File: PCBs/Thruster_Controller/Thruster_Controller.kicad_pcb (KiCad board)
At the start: 4 copper layers, 108 x 54 mm, 163 parts, among them J1 PHASE_A, J2 PHASE_B, J3 PHASE_C, J4 Big Conn, J5 Pogo Conn, J6 Conn CAN, J7 PWR_IN, Q1 SIZF906DT, Q2 SIZF906DT, Q3 SIZF906DT, SW1 SW_Push, SW2 SW_Push, U1 DRV8305, U2 RTQ2569-50GQW, U3 MCP2515, U4 LMR16006XDDC, U5 TMS320F28027F, U6 SN74LVC2G07, U7 SN74LVC2G07, U8 MCP2562, Y1 20MHz

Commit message: Layout
- Trying out different layout approaches
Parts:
- removed D4: D_Schottky_ALT, Diodes_SMD:D_SOD-123F
- removed D5, D6, D7, D8: BLUE, LEDs:LED_0805
- removed H3, H4: MountingHole, Mounting_Holes:MountingHole_3mm_Pad_Via
- removed J1: PHASE_A, MCU_Powertrain:3mm_Bullet_RA
- removed J2: PHASE_B, MCU_Powertrain:3mm_Bullet_RA
- removed J3: PHASE_C, MCU_Powertrain:3mm_Bullet_RA
- removed J4: Big Conn, MCU_Powertrain:2x05_Prog_Header
- removed J6: Conn CAN, MCU_Powertrain:70553-03
- removed L1: 15uH, MCU_Powertrain:Eaton_Inductor
- removed R23: 68.0k, Resistors_SMD:R_0603
- removed R24: 20.0k, Resistors_SMD:R_0603
- removed R31, R32, R33, R34: 330, Resistors_SMD:R_0805
- removed SW1, SW2: SW_Push, Buttons_Switches_SMD:SW_SPST_EVQQ2
- removed TP1, TP10, TP11, TP12, TP13, TP14, TP15, TP16, TP17, TP18, TP19, TP2, TP20, TP21, TP22, TP23, TP24, TP25, TP26, TP27, TP28, TP29, TP3, TP30, TP31, TP32, TP33, TP34, TP35, TP36, TP37, TP38, TP39, TP4, TP40, TP41, TP42, TP43, TP44, TP5, TP6, TP7, TP8, TP9: TestPoint, MCU_Powertrain:TestPoint_Loop_D1.80mm_Drill1.0mm_Beaded
- removed U4: LMR16006XDDC, TO_SOT_Packages_SMD:SOT-23-6
- removed U6, U7: SN74LVC2G07, Housings_SSOP:VSSOP-8_2.4x2.1mm_Pitch0.5mm
- added C43: 22uF, Capacitors_SMD:C_1812, F.Cu at (60.4, 89.2)
- added C44: 22uF, Capacitors_SMD:C_1812, F.Cu at (74.7, 74.9)
- added C45: 22uF, Capacitors_SMD:C_1812, F.Cu at (86.1, 91.7)
- added C46: 22uF, Capacitors_SMD:C_1812, F.Cu at (60.4, 84.4)
- added C47: 22uF, Capacitors_SMD:C_1812, F.Cu at (67.6, 74.9)
- added C48: 22uF, Capacitors_SMD:C_1812, F.Cu at (60.4, 79.7)
- C10, C11, C12: value 220uF -> 22uF; footprint Capacitors_SMD:CP_Elec_8x10.5 -> Capacitors_SMD:C_1812
- C13, C14, C15: footprint Capacitors_SMD:C_0805 -> Capacitors_SMD:C_1812; moved to F.Cu
- C31: footprint Capacitors_SMD:C_0805 -> Capacitors_SMD:C_1812
- C32: value 0.33uF -> 22uF; footprint Capacitors_SMD:C_0603 -> Capacitors_SMD:C_1812
- C33: value 0.1uF -> 22uF; footprint Capacitors_SMD:C_0603 -> Capacitors_SMD:C_1812; moved to F.Cu
- H1, H2: footprint Mounting_Holes:MountingHole_3mm_Pad_Via -> Mounting_Holes:MountingHole_2.2mm_M2
- J5, U1: moved to B.Cu
- J7: value PWR_IN -> PWRIN
- moved R7 171.7 mm to (264.6, 40.1), turned to 0 degrees
- moved D1 167.4 mm to (260.9, 40.1), turned to 0 degrees
- moved C16 158.8 mm to (236.4, 98.5)
- moved C17 158.8 mm to (234.3, 105.5)
- moved C27 158.8 mm to (229.3, 85.6)
- moved C3 158.8 mm to (231.9, 96.5)
- moved C30 158.8 mm to (186.1, 112.3)
- moved C34 158.8 mm to (216.3, 84.7)
- moved C39 158.8 mm to (182.2, 107.1)
- moved C4 158.8 mm to (235.6, 85.8)
- moved C6 158.8 mm to (234.2, 111.2)
- moved C7 158.8 mm to (234.2, 108.4)
- moved R10 158.8 mm to (229.9, 82.3)
- moved R14 158.8 mm to (235.6, 114.0)
- moved R19 158.8 mm to (237.6, 76.3)
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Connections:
- C13 pad 1: GND -> +BATT
- C13 pad 2: +BATT -> GND
- C14 pad 1: GND -> +BATT
- C14 pad 2: +BATT -> GND
- C15 pad 1: GND -> +BATT
- C15 pad 2: +BATT -> GND
- C31 pad 1: GND -> +BATT
- C31 pad 2: +3V3 -> GND
- C32 pad 1: Net-(C32-Pad1) -> +BATT
- C32 pad 2: Net-(C32-Pad2) -> GND
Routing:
- net +BATT: track 156.6 -> 0.00 mm, vias 31 -> 0
- net /GPIO28: track 112.5 -> 0.00 mm, vias 4 -> 0
- net /TDO: track 98.6 -> 0.00 mm, vias 2 -> 0
- net /TCK: track 82.7 -> 0.00 mm, vias 3 -> 0
- net /Powertrain/SPI_MOSI: track 81.2 -> 0.00 mm, vias 1 -> 0
- net /TMS: track 73.9 -> 0.00 mm, vias 1 -> 0
- net /Powertrain/SPI_MISO: track 71.7 -> 0.00 mm, vias 1 -> 0
- net /TI_MCU/ADCINA7: track 64.1 -> 0.00 mm
- net /Powertrain/SPI_CLK: track 63.5 -> 0.00 mm, vias 1 -> 0
- net /TDI: track 62.9 -> 0.00 mm, vias 4 -> 0
- net /TRST: track 62.2 -> 0.00 mm, vias 1 -> 0
- net /GPIO29: track 59.9 -> 0.00 mm, vias 1 -> 0
- net /Powertrain/PWRGD: track 58.2 -> 0.00 mm, vias 4 -> 0
- net /Powertrain/Phase_A: track 58.2 -> 0.00 mm, vias 45 -> 0
- net /TI_MCU/ADCINA3: track 57.9 -> 0.00 mm
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- removed copper zone on F.Cu, net +3V3
- removed copper zone on In2.Cu, net +3V3
- removed copper zone on B.Cu, net +BATT
- removed copper zone on F.Cu, net +BATT
- removed copper zone on In2.Cu, net +BATT
- removed copper zone on B.Cu, net /Powertrain/Phase_A
- removed copper zone on In1.Cu, net /Powertrain/Phase_A
- removed copper zone on In2.Cu, net /Powertrain/Phase_A
- removed copper zone on B.Cu, net /Powertrain/Phase_B
- removed copper zone on In1.Cu, net /Powertrain/Phase_B
- removed copper zone on In2.Cu, net /Powertrain/Phase_B
- removed copper zone on B.Cu, net /Powertrain/Phase_C
- removed copper zone on In1.Cu, net /Powertrain/Phase_C
- removed copper zone on In2.Cu, net /Powertrain/Phase_C
- removed copper zone on B.Cu, net /Powertrain/SL_A
- removed copper zone on B.Cu, net /Powertrain/SL_B
- removed copper zone on B.Cu, net /Powertrain/SL_C
- removed copper zone on B.Cu, net GND
- removed copper zone on F.Cu, net GND
- removed copper zone on In1.Cu, net GND
- removed copper zone on In2.Cu, net GND
- removed copper zone on F.Cu, net Net-(C32-Pad1)
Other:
- board size 108 x 54 mm -> 36 x 37.5 mm
- board text removed: "FOC Motor Controller Dev. Board"

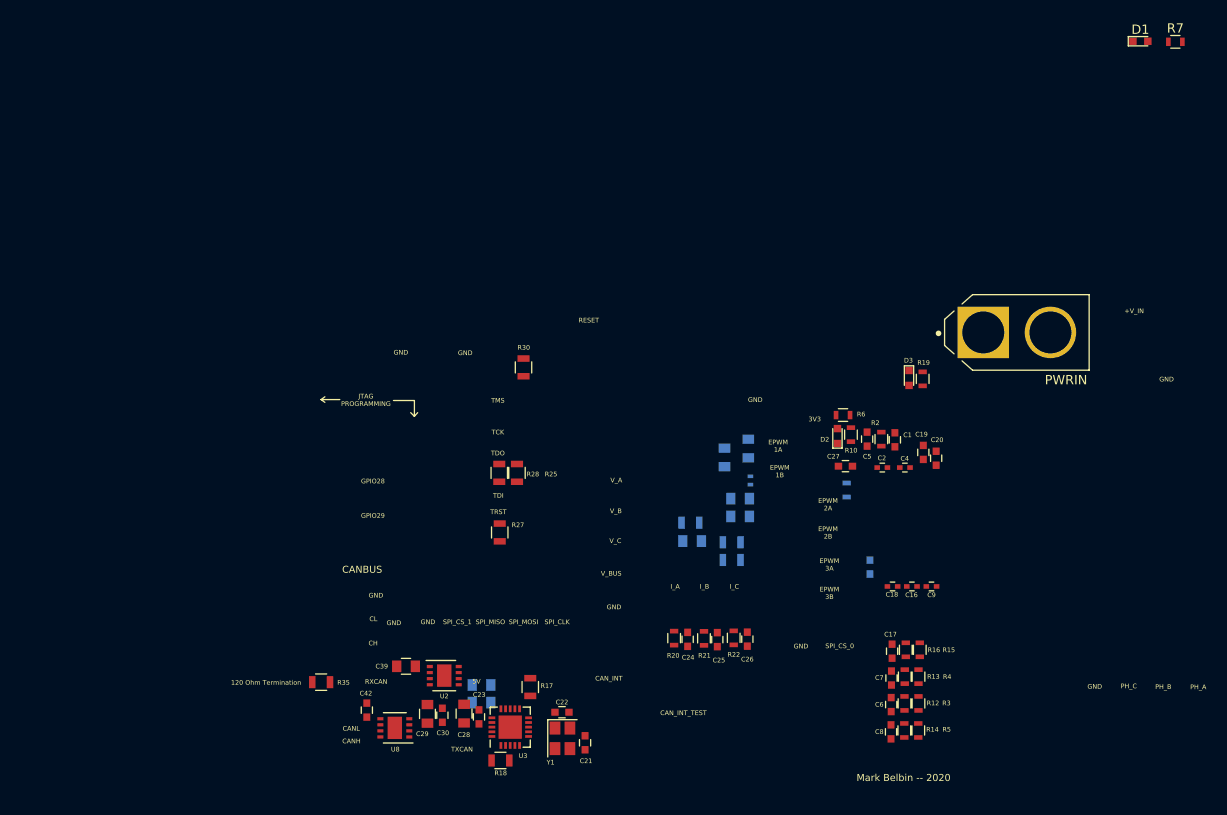
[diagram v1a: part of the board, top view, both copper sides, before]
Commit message: 3V3 Regulator
- Added in new 3V3 switching regulator, should save $$$ from the old one and about 1W versus a standard LDO
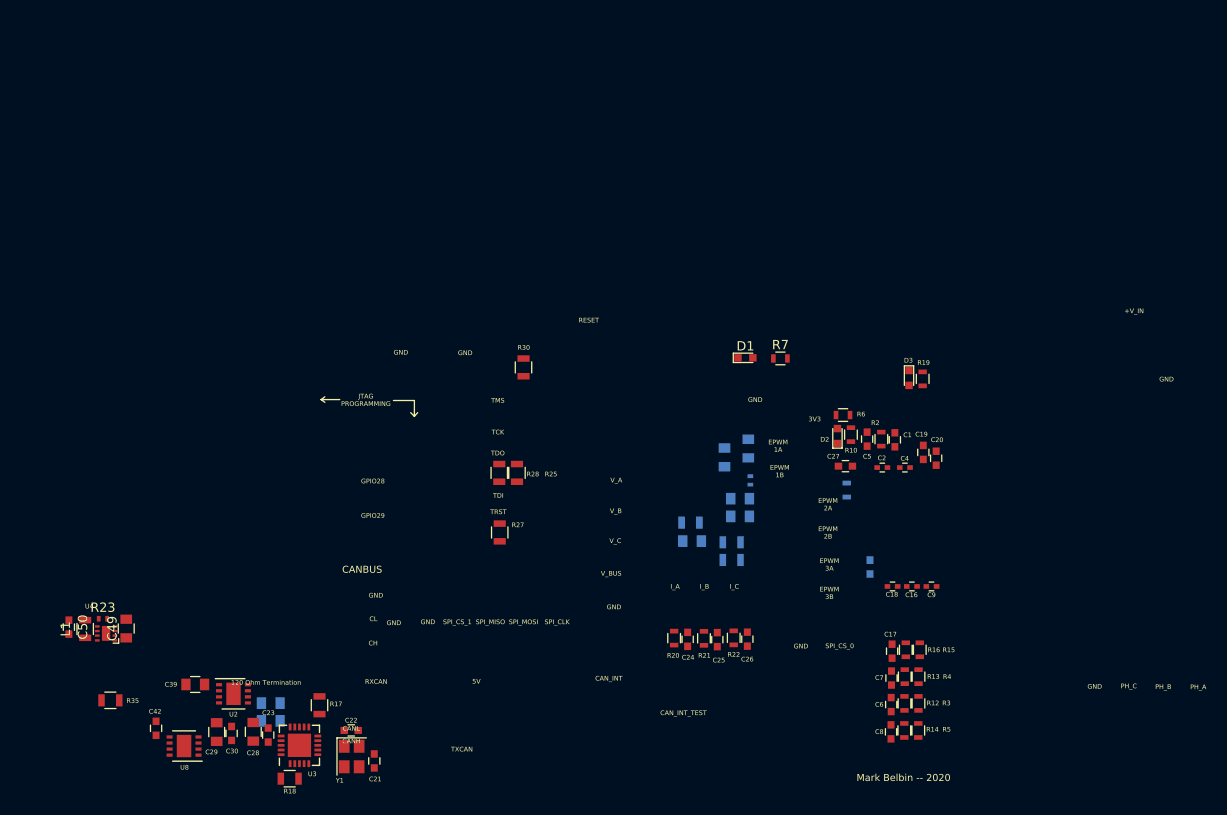
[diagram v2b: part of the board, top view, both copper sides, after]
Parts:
- removed J7: PWRIN, MCU_Powertrain:AMASS_XT60-M
- added C49: 10uF, Capacitors_SMD:C_0805, F.Cu at (152.2, 103.0)
- added C50: 22uF, Capacitors_SMD:C_0603, F.Cu at (146.0, 102.9)
- added L1: 2.2uH, Inductors_SMD:L_0805, F.Cu at (147.8, 103.1)
- added R23: 100k, Resistors_SMD:R_0402_NoSilk, F.Cu at (149.7, 102.0)
- added U4: TPS62172DSGR, Thruster_Controller:8-Pin_WSON, F.Cu at (150.0, 103.6)
- moved D1 54.3 mm to (218.5, 74.0)
- moved R7 54.3 mm to (222.3, 74.1)
- moved C30 22.7 mm to (163.4, 114.3)
- moved R35 22.7 mm to (150.4, 110.8)
- moved Y1 22.7 mm to (176.3, 116.8)
- moved C21 22.7 mm to (178.8, 117.2)
- moved C22 22.7 mm to (176.3, 114.0)
- moved C23 22.7 mm to (167.4, 114.5)
- moved C28 22.7 mm to (165.8, 114.1)
- moved C29 22.7 mm to (161.8, 114.2)
- moved C39 22.7 mm to (159.6, 109.0)
- moved C40 22.7 mm to (167.7, 113.0)
- moved C41 22.7 mm to (167.7, 111.0)
- moved C42 22.7 mm to (155.3, 113.8)
- moved R17 22.7 mm to (172.9, 111.3)
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
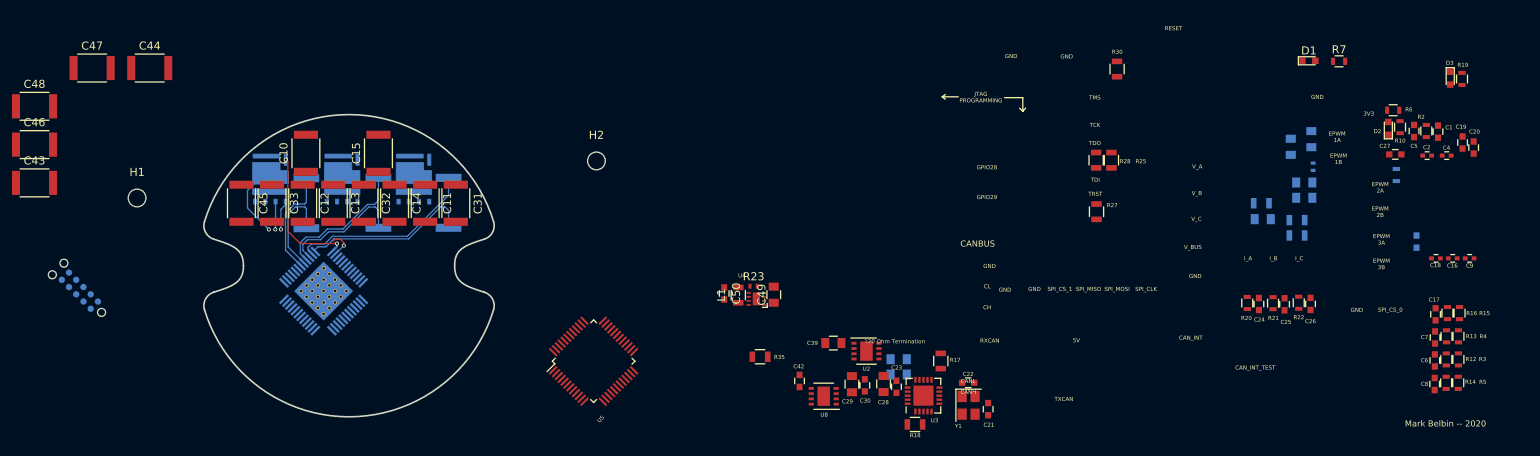
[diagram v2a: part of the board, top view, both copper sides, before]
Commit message: More Layout and Routing
- Powertrain is mostly done, very tight and the phase and bus pads are sized and placed!
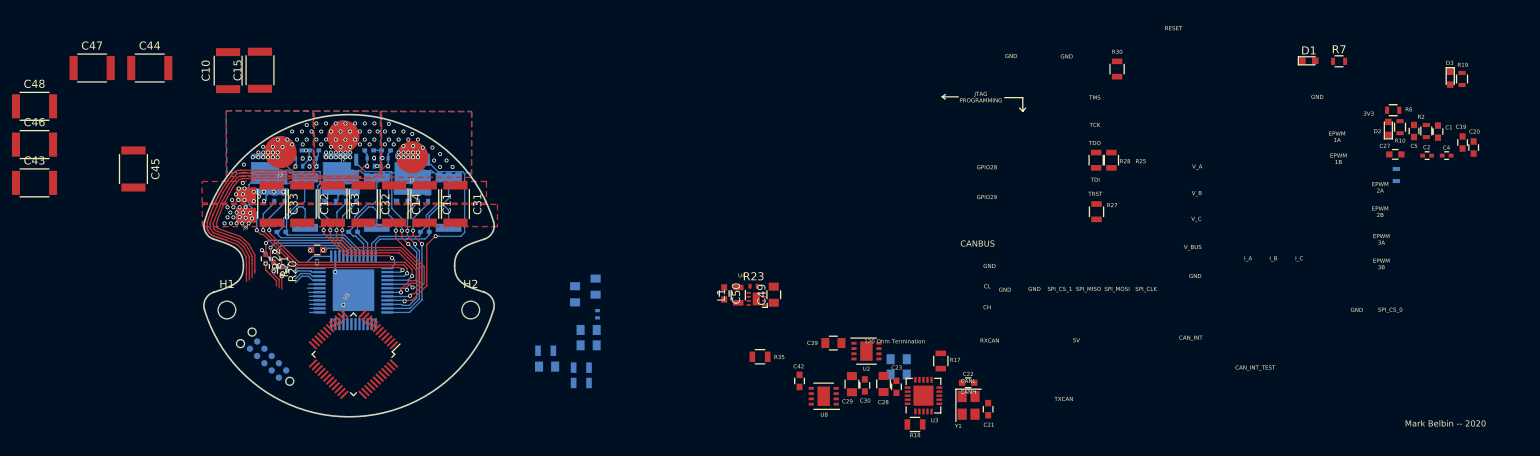
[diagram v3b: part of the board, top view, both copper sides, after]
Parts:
- added J1: PHASE_A, Thruster_Controller:Phase_Pad, F.Cu at (107.3, 86.0)
- added J2: PHASE_B, Thruster_Controller:Phase_Pad, F.Cu at (98.8, 83.4)
- added J3: PHASE_C, Thruster_Controller:Phase_Pad, F.Cu at (91.0, 85.3)
- added J7: Conn_01x01, Thruster_Controller:Bus_Pad, F.Cu at (86.7, 90.7)
- added J8: Conn_01x01, Thruster_Controller:Bus_Pad, F.Cu at (86.7, 93.2)
- C16, C18, C9: moved to B.Cu
- C17, C24, C25, C26, C6, C7, C8: footprint Capacitors_SMD:C_0603 -> Capacitors_SMD:C_0402; moved to B.Cu
- C3: moved to F.Cu
- Q1, Q2, Q3: footprint MCU_Powertrain:SIZF906DT -> Thruster_Controller:SIZF906DT
- R12, R13, R14, R15, R16, R3, R4, R5: footprint Resistors_SMD:R_0603 -> Resistors_SMD:R_0402; moved to B.Cu
- R20, R21, R22: footprint Resistors_SMD:R_0603 -> Resistors_SMD:R_0402
- U1: footprint MCU_Powertrain:DRV8305 -> Thruster_Controller:DRV8305
- moved R4 145.5 mm to (93.2, 86.1), turned to 180 degrees
- moved R13 143.9 mm to (93.2, 87.1), turned to 0 degrees
- moved R15 143.4 mm to (95.0, 87.1), turned to 0 degrees
- moved C18 143.3 mm to (91.0, 95.2)
- moved C7 143.1 mm to (93.0, 85.2), turned to 0 degrees
- moved R16 142.1 mm to (95.0, 86.1), turned to 180 degrees
- moved C17 140.6 mm to (95.2, 85.2), turned to 180 degrees
- moved R3 137.2 mm to (102.2, 86.1), turned to 180 degrees
- moved C16 136.5 mm to (100.0, 95.2)
- moved C3 136.4 mm to (95.5, 97.5), turned to 180 degrees
- moved R5 136.1 mm to (103.8, 86.1), turned to 0 degrees
- moved R12 135.6 mm to (102.2, 87.1), turned to 0 degrees
- moved C6 134.8 mm to (102.0, 85.2), turned to 0 degrees
- moved R14 134.4 mm to (103.8, 87.1), turned to 180 degrees
- moved C8 133.3 mm to (104.0, 85.2), turned to 180 degrees
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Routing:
- net /TI_MCU/ADCINA7: track 0.00 -> 36.3 mm, vias 0 -> 1
- net /TI_MCU/ADCINA3: track 0.00 -> 34.7 mm, vias 0 -> 1
- net /TI_MCU/ADCINA0: track 0.00 -> 29.2 mm, vias 0 -> 1
- net /Powertrain/GL_A: track 0.00 -> 28.8 mm, vias 0 -> 2
- net /Powertrain/SL_B: track 1.11 -> 28.7 mm, vias 0 -> 2
- net /TI_MCU/ADCINA1: track 0.00 -> 27.1 mm, vias 0 -> 1
- net /Powertrain/GL_B: track 0.00 -> 26.4 mm, vias 0 -> 2
- net /Powertrain/GH_C: track 3.70 -> 28.4 mm, vias 1 -> 2
- net /Powertrain/SH_C: track 3.47 -> 27.8 mm, vias 1 -> 2
- net /Powertrain/GH_B: track 0.00 -> 23.3 mm, vias 0 -> 2
- net /Powertrain/SH_B: track 0.00 -> 23.0 mm, vias 0 -> 2
- net /Powertrain/SL_A: track 1.11 -> 23.3 mm, vias 0 -> 2
- net GND: track 3.07 -> 22.6 mm, vias 0 -> 26
- net /Powertrain/GH_A: track 0.00 -> 18.6 mm, vias 0 -> 2
- net /Powertrain/SL_C: track 13.8 -> 32.1 mm
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- added copper zone on In2.Cu, net +3V3
- added copper zone on B.Cu, net +BATT
- added copper zone on F.Cu, net +BATT
- added copper zone on In2.Cu, net +BATT
- added copper zone on B.Cu, net /Powertrain/Phase_A
- added copper zone on F.Cu, net /Powertrain/Phase_A
- added copper zone on B.Cu, net /Powertrain/Phase_B
- added copper zone on F.Cu, net /Powertrain/Phase_B
- added copper zone on B.Cu, net /Powertrain/Phase_C
- added copper zone on F.Cu, net /Powertrain/Phase_C
- added copper zone on B.Cu, net /Powertrain/SL_A
- added copper zone on B.Cu, net /Powertrain/SL_B
- added copper zone on B.Cu, net /Powertrain/SL_C
- added copper zone on F.Cu, net GND
- added copper zone on In1.Cu, net GND
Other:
- rule solder_mask_min_width: 0.25 -> 0.1

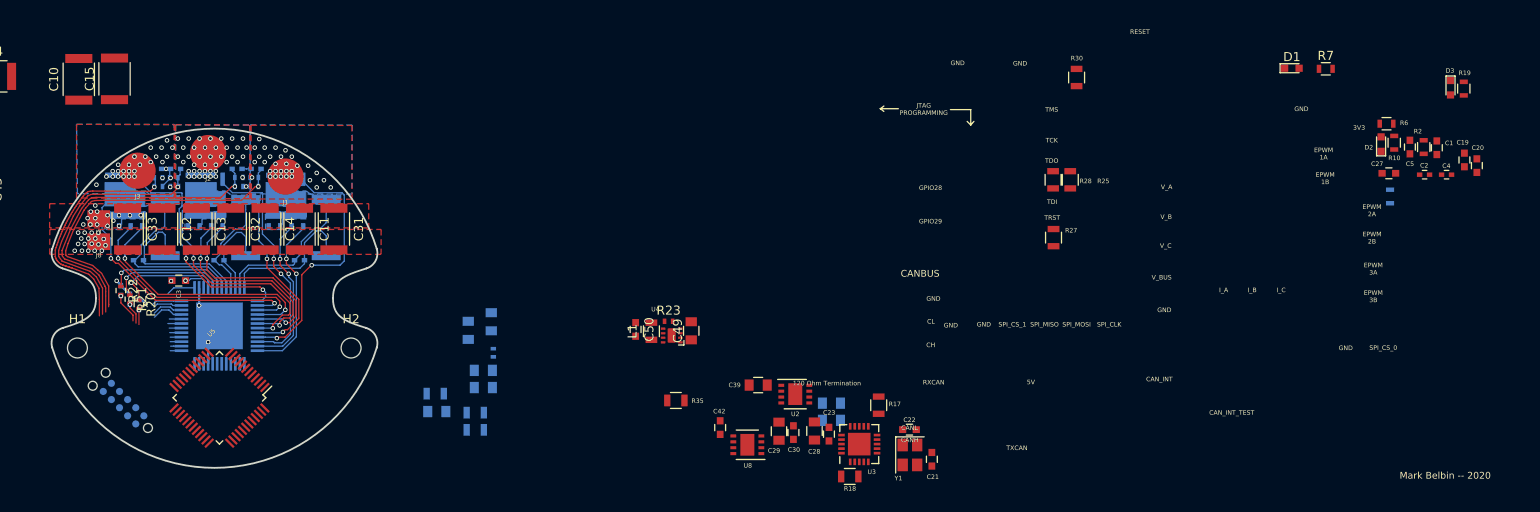
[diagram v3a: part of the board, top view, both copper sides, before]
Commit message: More Layout + Routing
- Added 3V3 converter
- Moved DRV passives to directly underneath DRV chip on top layer
- Fit power indication LEDs!
- Think there should be enough space for everything! Routing to the left of TI chip and CAN controller to the right
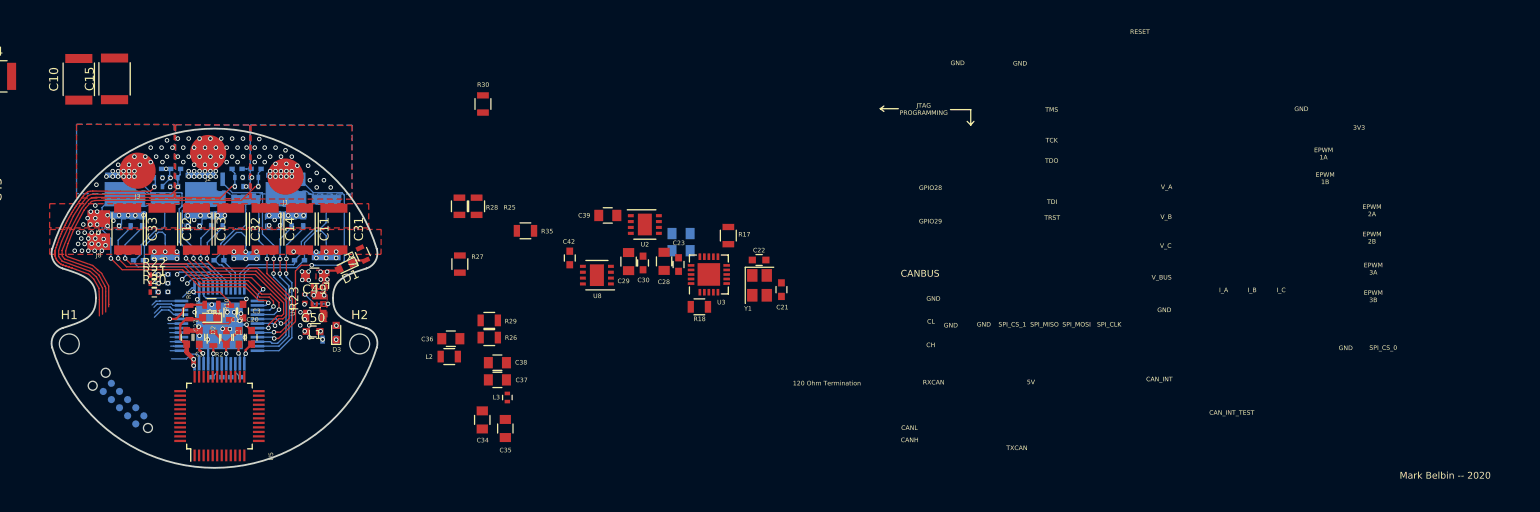
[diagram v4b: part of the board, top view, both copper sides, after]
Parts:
- C2, C4, R19: moved to B.Cu
- C34, C35, C36, C37, C38, L2, L3, R1, R26, R29: moved to F.Cu
- H1, H2: footprint Mounting_Holes:MountingHole_2.2mm_M2 -> Thruster_Controller:MountingHole_M2
- moved C19 136.9 mm to (102.2, 103.8)
- moved C20 136.8 mm to (103.5, 103.8)
- moved C4 135.7 mm to (101.8, 108.2)
- moved C5 135.5 mm to (97.8, 103.8)
- moved R2 135.5 mm to (99.3, 103.9), turned to 270 degrees
- moved C1 135.4 mm to (100.8, 103.8)
- moved C2 135.4 mm to (99.7, 108.2)
- moved C27 134.1 mm to (96.4, 103.8), turned to 90 degrees
- moved R6 134.0 mm to (96.7, 101.0), turned to 90 degrees
- moved R10 132.0 mm to (99.1, 100.2), turned to 180 degrees
- moved D2 130.9 mm to (98.9, 101.6), turned to 180 degrees
- moved R1 128.9 mm to (101.2, 101.0), turned to 90 degrees
- moved R19 128.4 mm to (112.2, 104.0), turned to 180 degrees
- moved D3 126.1 mm to (112.9, 103.2), turned to 90 degrees
- moved R7 108.4 mm to (115.8, 94.6), turned to 115 degrees
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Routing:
- net +3V3: track 0.00 -> 12.9 mm, vias 0 -> 12
- net /Powertrain/ISEN_A_DRV: track 12.2 -> 3.46 mm
- net +BATT: track 0.00 -> 8.33 mm, vias 16 -> 38
- net /Powertrain/ISEN_B_DRV: track 12.5 -> 4.25 mm
- net GND: track 22.6 -> 30.7 mm, vias 26 -> 66
- net /Powertrain/ISEN_C_DRV: track 13.1 -> 5.37 mm
- net /GPIO28: track 1.35 -> 6.02 mm, vias 0 -> 1
- net /TI_MCU/GPIO7: track 0.00 -> 4.22 mm
- net /Powertrain/PWRGD: track 3.22 -> 7.20 mm, vias 0 -> 1
- net Net-(C3-Pad1): track 3.03 -> 6.50 mm
- net /TI_MCU/ADCINB7: track 3.31 -> 0.06 mm
- net Net-(R23-Pad2): track 0.00 -> 3.22 mm, vias 0 -> 2
- net Net-(C20-Pad1): track 0.00 -> 2.51 mm, vias 0 -> 1
- net Net-(C5-Pad1): track 0.00 -> 2.43 mm, vias 0 -> 1
- net Net-(C19-Pad2): track 0.00 -> 2.26 mm, vias 0 -> 1
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- added copper zone on In1.Cu, net /Powertrain/Phase_A
- added copper zone on In2.Cu, net /Powertrain/Phase_A
- added copper zone on In1.Cu, net /Powertrain/Phase_B
- added copper zone on In2.Cu, net /Powertrain/Phase_B
- added copper zone on In1.Cu, net /Powertrain/Phase_C
- added copper zone on In2.Cu, net /Powertrain/Phase_C
- added copper zone on In2.Cu, net GND
- added copper zone on F.Cu, net Net-(L1-Pad1)
